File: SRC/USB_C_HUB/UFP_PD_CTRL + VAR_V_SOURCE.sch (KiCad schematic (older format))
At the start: 48 parts, among them IC5 STUSB4700YQTR, Q5 BSH105,215, Q6 BSH105,215, Q7 RQ5E025ATTCL, Q8 BSH105,215, Q9 BSH105,215, U14 LM3489QMM, U15 CWDM3011P, U16 SQJ951EP

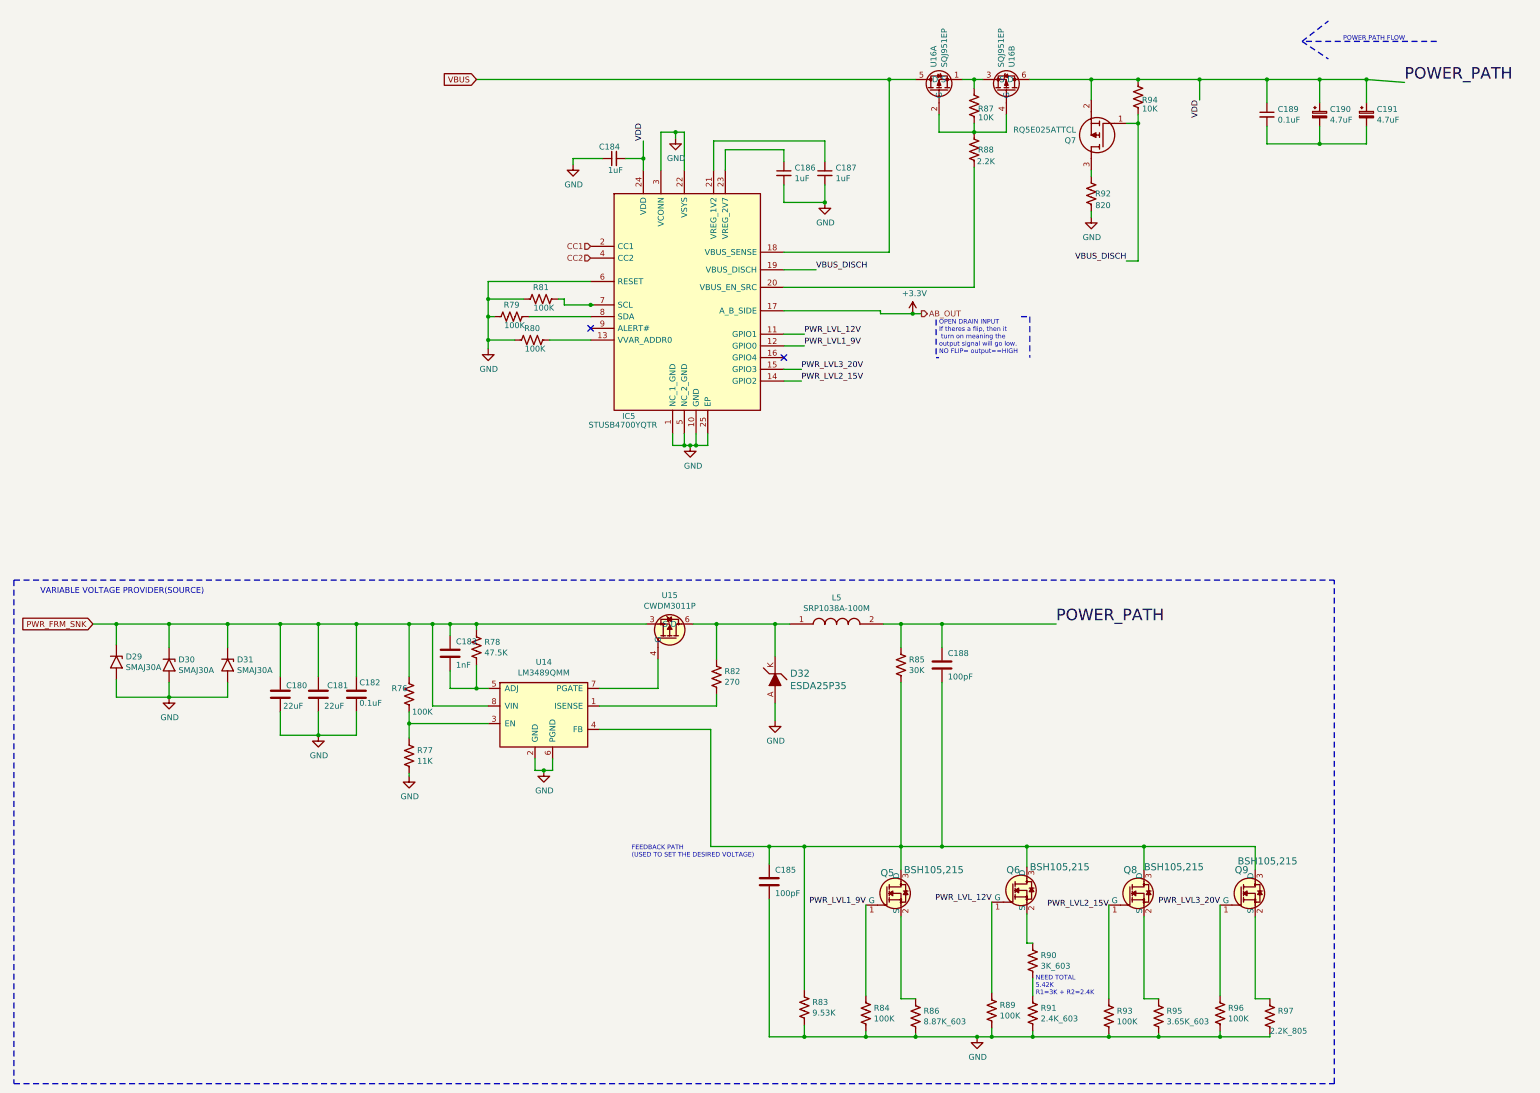
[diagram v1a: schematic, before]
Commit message: schematic capture and footprint assignment complete. Pending approval
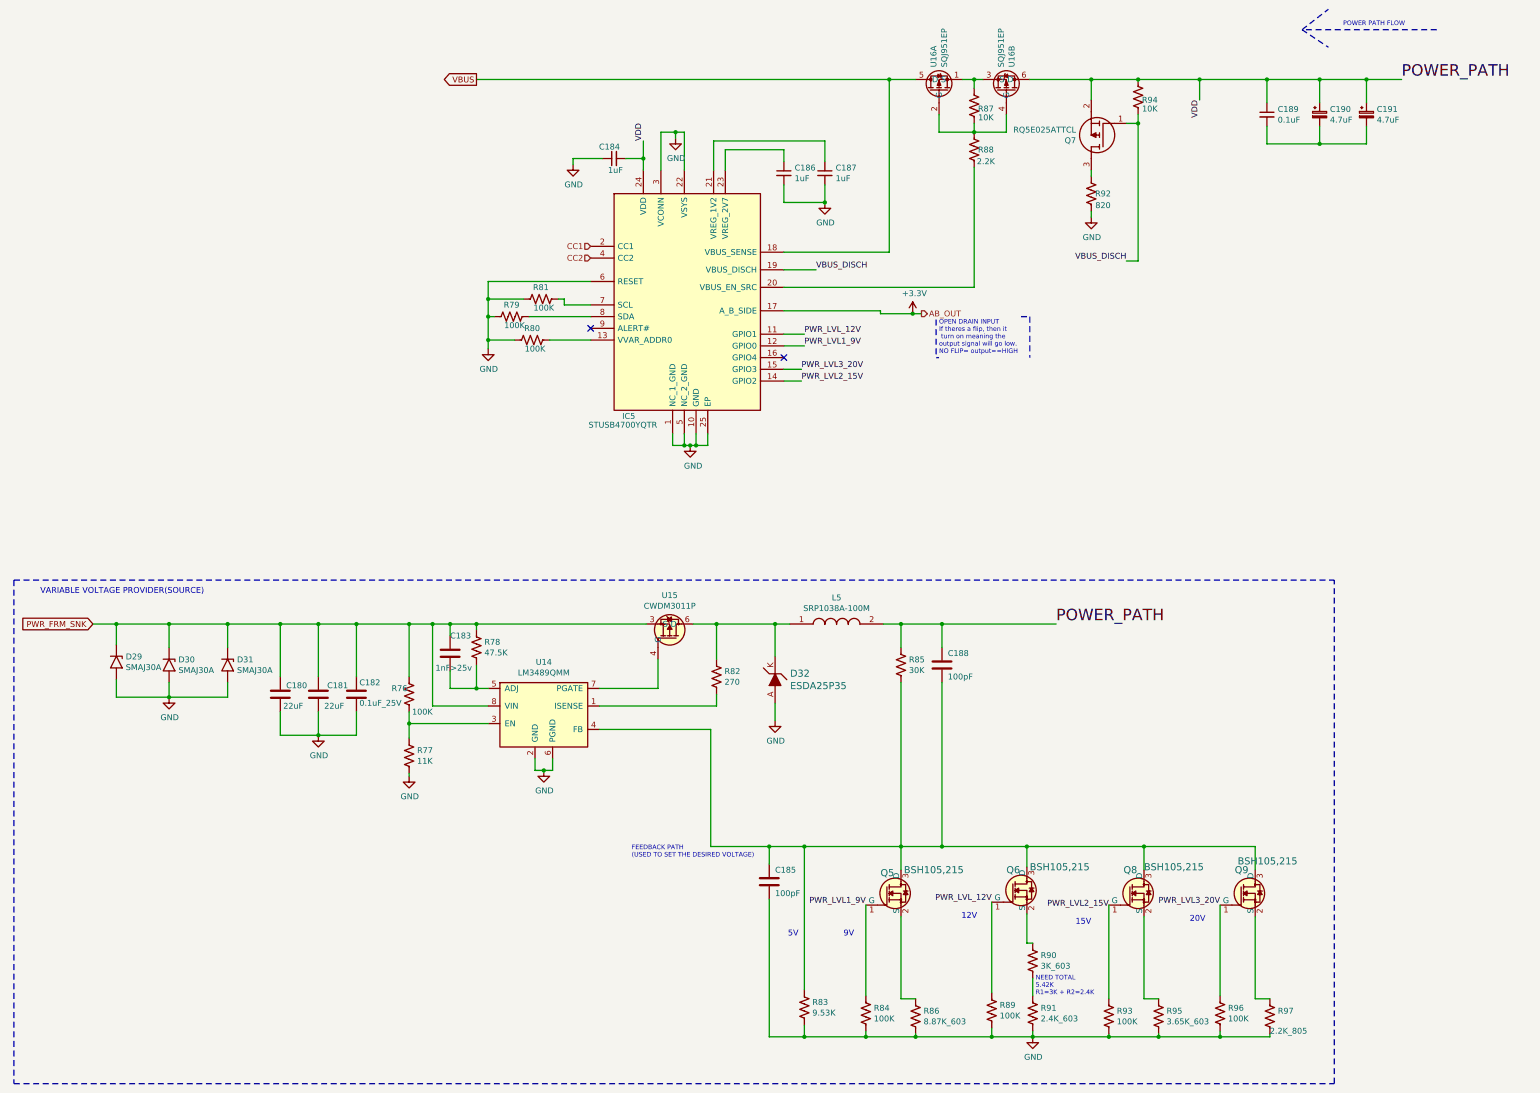
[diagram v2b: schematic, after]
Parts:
- C180, C181: footprint (none) -> Capacitor_SMD:C_0805_2012Metric; Mfr No. (none) -> GMC21X5R226M25NT
- C182: value 0.1uF -> 0.1uF_25V; footprint (none) -> Capacitor_SMD:C_0402_1005Metric; Mfr No. (none) -> GMC04X7R104K25NT
- C183: value 1nF -> 1nF>25v; footprint (none) -> Capacitor_SMD:C_0402_1005Metric; Mfr No. (none) -> CC0402KRX7R9BB102
- C184, C185, C186, C187, C188, C189: footprint (none) -> Capacitor_SMD:C_0402_1005Metric
- C190, C191: footprint (none) -> Capacitor_Tantalum_SMD:CP_EIA-3528-21_Kemet-B
- D29, D30, D31: footprint Diode_SMD:D_SMB -> Diode_SMD:D_SMA
- R76, R77, R78, R86, R87, R88, R90, R91, R92, R94, R95, R97: footprint (none) -> Resistor_SMD:R_0603_1608Metric
- R79, R80, R81, R84, R89, R93, R96: footprint (none) -> Resistor_SMD:R_0402_1005Metric
- R82: footprint (none) -> Resistor_SMD:R_0603_1608Metric; Mfr No. (none) -> HPCR0603F270RK9
- R83: footprint (none) -> Resistor_SMD:R_0603_1608Metric; Mfr No. (none) -> 0603WAF9531T5E
- R85: footprint (none) -> Resistor_SMD:R_0603_1608Metric; Mfr No. (none) -> 0603WAF3002T5E
- U14: footprint (none) -> footprints:SOP65P490X110-8N
- U15: footprint (none) -> footprints:SOIC127P600X175-8N
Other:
- note added: "12V"
- note added: "15V"
- note added: "20V"
- note added: "5V"
- note added: "9V"
